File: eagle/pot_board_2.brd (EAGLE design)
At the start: 100 x 80 mm, 18 parts, among them IC1 4067N, X2 22-23-2081

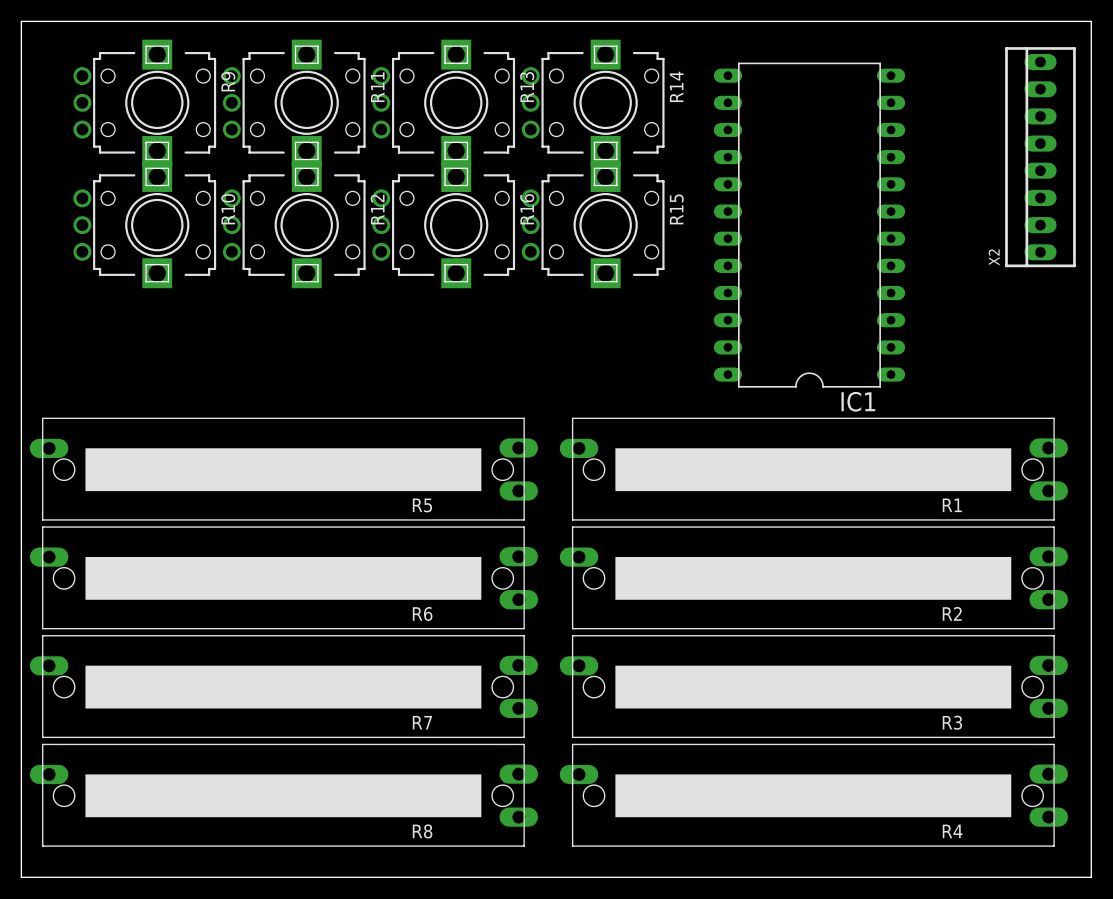
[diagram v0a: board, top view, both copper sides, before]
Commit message: standard connector for display
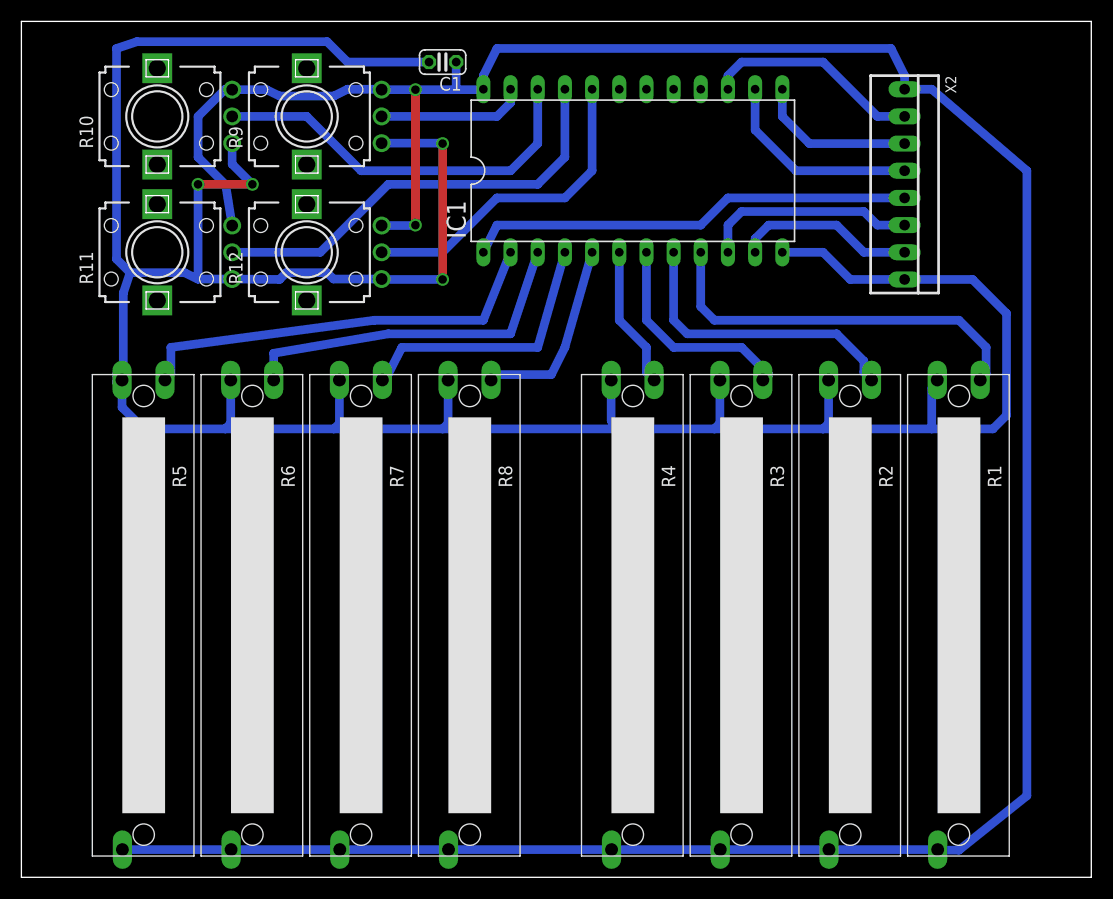
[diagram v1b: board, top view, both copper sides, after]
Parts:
- removed R13, R14, R15, R16: EVUF2A, pot:EVUF
- added C1: 100n, rcl:C025-024X044
- moved R4 55.7 mm to (57.1, 47.0), turned to 180 degrees
- moved R3 41.3 mm to (67.3, 47.0), turned to 180 degrees
- moved R8 39.7 mm to (41.9, 47.0), turned to 180 degrees
- moved R5 36.7 mm to (11.4, 47.0), turned to 180 degrees
- moved R7 32.9 mm to (31.8, 47.0), turned to 180 degrees
- moved R6 31.8 mm to (21.6, 47.0), turned to 180 degrees
- moved R2 26.9 mm to (77.5, 47.0), turned to 180 degrees
- moved R11 19.8 mm to (12.7, 58.4), turned to 90 degrees
- moved IC1 17.3 mm to (57.1, 66.0), turned to 0 degrees
- moved R9 14.0 mm to (26.7, 71.1), turned to 90 degrees
- moved X2 13.0 mm to (82.5, 64.8), turned to 270 degrees
- moved R1 12.6 mm to (87.6, 47.0), turned to 180 degrees
- moved R10 10.2 mm to (12.7, 71.1), turned to 90 degrees
- moved R12 2.54 mm to (26.7, 58.4), turned to 90 degrees
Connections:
- removed net N$16: X2.3
- new net N$9: IC1.15, X2.2
- net +5V: now also C1.1; no longer R13.3, R14.3, R15.3, R16.3
- net GND: now also C1.2; no longer R13.1, R14.1, R15.1, R16.1
- net N$12: now also IC1.11; no longer IC1.10
- net N$13: now also IC1.10; no longer IC1.11
- net N$14: now also X2.4; no longer X2.5
- net N$15: now also X2.3; no longer X2.4
- net N$17: now also X2.5; no longer X2.2
- net N$21: no longer R13.2
- net N$22: no longer R16.2
- net N$23: no longer R15.2
- net N$24: no longer R14.2
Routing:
- net GND: track 0.00 -> 283.9 mm, vias 0 -> 4
- net +5V: track 0.00 -> 261.9 mm, vias 0 -> 2
- net N$17: track 0.00 -> 42.0 mm
- net N$19: track 0.00 -> 41.1 mm
- net N$8: track 0.00 -> 39.5 mm
- net N$18: track 0.00 -> 36.8 mm
- net N$1: track 0.00 -> 36.6 mm
- net N$7: track 0.00 -> 32.8 mm
- net N$20: track 0.00 -> 30.4 mm
- net N$2: track 0.00 -> 27.8 mm
- net N$6: track 0.00 -> 25.5 mm
- net N$3: track 0.00 -> 20.6 mm
- net N$9: track 0.00 -> 20.4 mm
- net N$13: track 0.00 -> 20.1 mm
- net N$14: track 0.00 -> 19.4 mm
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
